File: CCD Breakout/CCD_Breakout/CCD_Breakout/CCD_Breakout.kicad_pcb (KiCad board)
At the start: 2 copper layers, 105.7 x 25.4 mm, 33 parts, among them U1 CCD, U3 ADC-MCP33151, U5 74HC541PW_118, U8 OPA4322AIPWR

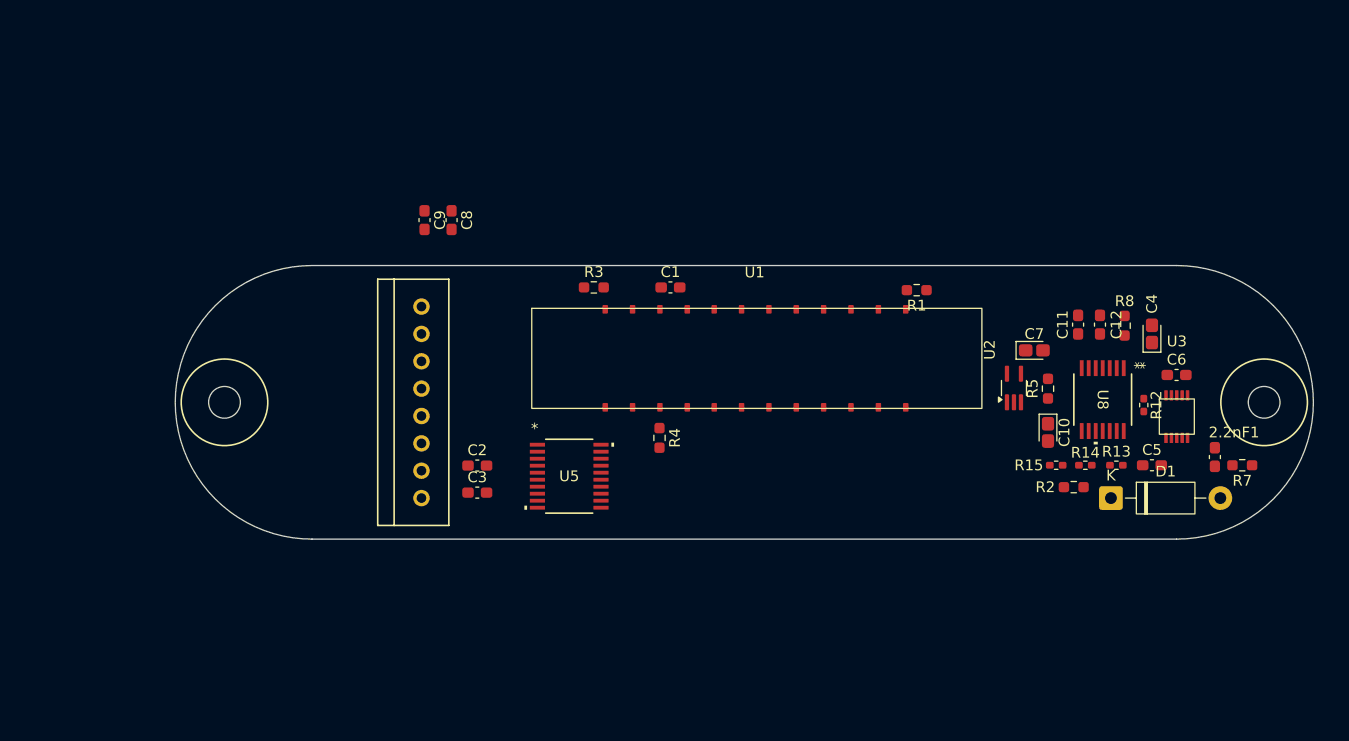
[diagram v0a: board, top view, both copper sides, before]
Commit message: CCD Positional Layout
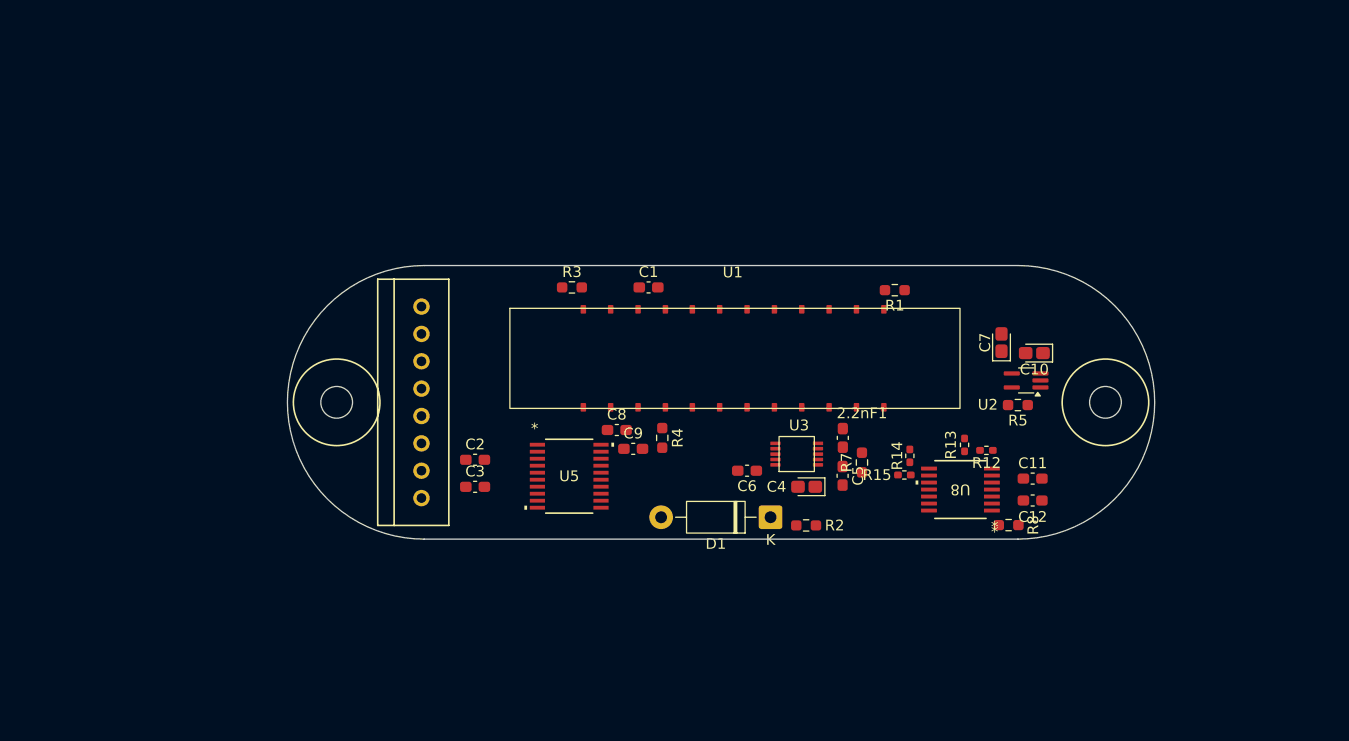
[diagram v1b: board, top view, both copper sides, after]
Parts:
- moved C6 40.9 mm to (147.8, 93.0), turned to 180 degrees
- moved U3 35.5 mm to (152.4, 91.4), turned to 90 degrees
- moved R7 35.3 mm to (158.5, 92.2), turned to 90 degrees
- moved C4 35.1 mm to (153.4, 94.5), turned to 180 degrees
- moved 2.2nF1 34.6 mm to (156.7, 89.9)
- moved D1 31.6 mm to (150.0, 97.3), turned to 180 degrees
- moved C9 28.7 mm to (137.3, 90.9), turned to 0 degrees
- moved C5 28.7 mm to (156.7, 93.4), turned to -90 degrees
- moved R2 25.1 mm to (153.3, 98.0), turned to 180 degrees
- moved C8 24.8 mm to (135.7, 89.2), turned to 0 degrees
- moved R8 21.4 mm to (172.1, 98.0), turned to 180 degrees
- moved C12 17.5 mm to (174.3, 95.7), turned to 0 degrees
- moved R14 16.3 mm to (162.9, 91.6), turned to 90 degrees
- moved U8 15.6 mm to (167.6, 94.7), turned to 180 degrees
- moved R12 15.2 mm to (170.1, 91.1), turned to 180 degrees
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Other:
- board size 105.7 x 25.4 mm -> 80.5 x 25.4 mm

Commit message: CCD Layout Traces
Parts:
- moved D1 0.83 mm to (149.4, 96.8)
- moved R2 0.83 mm to (152.7, 97.5)
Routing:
- net +5V: track 0.00 -> 164.6 mm, vias 0 -> 22
- net /ADC/OUT: track 0.00 -> 45.0 mm, vias 0 -> 3
- net +3V3: track 0.00 -> 43.6 mm, vias 0 -> 3
- net /ADC/CLK2: track 0.00 -> 43.1 mm, vias 0 -> 1
- net /CCD/EOSb: track 0.00 -> 41.1 mm, vias 0 -> 4
- net /CCD/opINA+: track 0.00 -> 25.9 mm, vias 0 -> 4
- net /CCD/EOS: track 0.00 -> 23.0 mm, vias 0 -> 1
- net /CCD/STb: track 0.00 -> 21.1 mm
- net /CCD/Trigb: track 0.00 -> 19.6 mm, vias 0 -> 2
- net /ADC/TRIG: track 0.00 -> 17.9 mm, vias 0 -> 2
- net /CCD/ST: track 0.00 -> 17.5 mm, vias 0 -> 1
- net /ADC/opIND+: track 0.00 -> 17.1 mm, vias 0 -> 3
- net /CCD/Videob: track 0.00 -> 15.6 mm, vias 0 -> 2
- net /ADC/opIND-: track 0.00 -> 14.1 mm, vias 0 -> 4
- net /CCD/opINB+: track 0.00 -> 13.9 mm
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- added copper zone on B.Cu, net GND
- added copper zone on F.Cu, net GND

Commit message: Added Reverse Voltage Protection
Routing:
- net (no net): vias 0 -> 2
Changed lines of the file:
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@@
+	)
+	(via
+		(at 80.772 51.562)
+		(size 0.6)
+		(drill 0.3)
+		(layers "F.Cu" "B.Cu")
+		(net 0)
+	)
+	(via
+		(at 201.422 75.184)
+		(size 0.6)
+		(drill 0.3)
+		(layers "F.Cu" "B.Cu")
+		(net 0)
 	)
 	(via

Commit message: Push
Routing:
- net GND: vias 46 -> 45
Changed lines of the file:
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@@
 		(layer "Edge.Cuts")
 	)
+	(dimension
+		(type orthogonal)
+		(layer "Dwgs.User")
+		(pts
+			(xy 185.674 86.614) (xy 105.156 86.614)
+		)
+		(height -18.034)
+		(orientation 0)
+		(format
+			(prefix "")
+			(suffix "")
+			(units 3)
+			(units_format 0)
+			(precision 4)
+			(suppress_zeroes yes)
+		)
+		(style
+			(thickness 0.1)
+			(arrow_length 1.27)
+			(text_position_mode 0)
+			(arrow_direction outward)
+			(extension_height 0.58642)
+			(extension_offset 0.5)
+			(keep_text_aligned yes)
+		)
+		(gr_text "3170"
+			(at 145.415 67.43 0)
+			(layer "Dwgs.User")
+			(effects
+				(font
+					(size 1 1)
+					(thickness 0.15)
+				)
+			)
+		)
+	)
+	(dimension
+		(type orthogonal)
+		(layer "Dwgs.User")
+		(pts
+			(xy 145.415 99.314) (xy 146.704 73.914)
+		)
+		(height 46.863)
+		(orientation 1)
+		(format
+			(prefix "")
+			(suffix "")
+			(units 3)
+			(units_format 0)
+			(precision 4)
+			(suppress_zeroes yes)
+		)
+		(style
+			(thickness 0.1)
+			(arrow_length 1.27)
+			(text_position_mode 0)
+			(arrow_direction outward)
+			(extension_height 0.58642)
+			(extension_offset 0.5)
+			(keep_text_aligned yes)
+		)
+		(gr_text "1000"
+			(at 191.128 86.614 90)
+			(layer "Dwgs.User")
+			(effects
+				(font
+					(size 1 1)
+					(thickness 0.15)
+				)
+			)
+		)
+	)
+	(dimension
+		(type orthogonal)
+		(layer "Dwgs.User")
+		(pts
+			(xy 181.102 86.614) (xy 109.728 86.614)
+		)
+		(height -22.352)
+		(orientation 0)
+		(format
+			(prefix "")
+			(suffix "")
+			(units 3)
+			(units_format 0)
+			(precision 4)
+			(suppress_zeroes yes)
+		)
+		(style
+			(thickness 0.1)
+			(arrow_length 1.27)
+			(text_position_mode 0)
+			(arrow_direction outward)
+			(extension_height 0.58642)
+			(extension_offset 0.5)
+			(keep_text_aligned yes)
+		)
+		(gr_text "2810"
+			(at 145.415 63.112 0)
+			(layer "Dwgs.User")
+			(effects
+				(font
+					(size 1 1)
+					(thickness 0.15)
+				)
+			)
+		)
+	)
 	(via
 		(at 80.772 51.562)
@@
 	)
 	(via
-		(at 179.324 80.01)
-		(size 0.6)
-		(drill 0.3)
-		(layers "F.Cu" "B.Cu")
-		(free yes)
-		(net 1)
-	)
-	(via
-		(at 126.492 94.742)
+		(at 179.324 79.502)
+		(size 0.6)
+		(drill 0.3)
+		(layers "F.Cu" "B.Cu")
+		(free yes)
+		(net 1)
+	)
+	(via
+		(at 126.238 95.504)
 		(size 0.6)
 		(drill 0.3)
@@
 	)
 	(via
-		(at 123.19 96.52)
+		(at 123.19 95.504)
 		(size 0.6)
 		(drill 0.3)
@@
 	)
 	(via
-		(at 154.686 89.154)
+		(at 154.686 88.392)
 		(size 0.6)
 		(drill 0.3)
@@
 	)
 	(via
-		(at 165.354 89.154)
+		(at 165.354 88.392)
 		(size 0.6)
 		(drill 0.3)
@@
 	)
 	(via
-		(at 179.832 93.218)
+		(at 179.324 93.218)
 		(size 0.6)
 		(drill 0.3)
@@
 	)
 	(via
-		(at 147.066 88.646)
-		(size 0.6)
-		(drill 0.3)
-		(layers "F.Cu" "B.Cu")
-		(free yes)
-		(net 1)
-	)
-	(via
-		(at 169.672 88.138)
+		(at 147.066 88.392)
+		(size 0.6)
+		(drill 0.3)
+		(layers "F.Cu" "B.Cu")
+		(free yes)
+		(net 1)
+	)
+	(via
+		(at 169.672 88.392)
 		(size 0.6)
 		(drill 0.3)
@@
 	)
 	(via
-		(at 141.224 91.948)
-		(size 0.6)
-		(drill 0.3)
-		(layers "F.Cu" "B.Cu")
-		(free yes)
-		(net 1)
-	)
-	(via
-		(at 163.83 82.55)
+		(at 143.51 91.948)
+		(size 0.6)
+		(drill 0.3)
+		(layers "F.Cu" "B.Cu")
+		(free yes)
+		(net 1)
+	)
+	(via
+		(at 163.83 82.296)
 		(size 0.6)
 		(drill 0.3)
@@
 	)
 	(via
-		(at 163.83 76.2)
-		(size 0.6)
-		(drill 0.3)
-		(layers "F.Cu" "B.Cu")
-		(free yes)
-		(net 1)
-	)
-	(via
-		(at 170.18 76.2)
-		(size 0.6)
-		(drill 0.3)
-		(layers "F.Cu" "B.Cu")
-		(free yes)
-		(net 1)
-	)
-	(via
-		(at 174.498 90.17)
+		(at 163.83 75.946)
+		(size 0.6)
+		(drill 0.3)
+		(layers "F.Cu" "B.Cu")
+		(free yes)
+		(net 1)
+	)
+	(via
+		(at 170.18 75.946)
+		(size 0.6)
+		(drill 0.3)
+		(layers "F.Cu" "B.Cu")
+		(free yes)
+		(net 1)
+	)
+	(via
+		(at 174.498 88.392)
 		(size 0.6)
 		(drill 0.3)
@@
 	)
 	(via
-		(at 151.13 88.9)
-		(size 0.6)
-		(drill 0.3)
-		(layers "F.Cu" "B.Cu")
-		(free yes)
-		(net 1)
-	)
-	(via
-		(at 143.51 90.424)
+		(at 151.13 88.392)
+		(size 0.6)
+		(drill 0.3)
+		(layers "F.Cu" "B.Cu")
+		(free yes)
+		(net 1)
+	)
+	(via
+		(at 143.51 88.392)
 		(size 0.6)
 		(drill 0.3)
@@
 	)
 	(via
-		(at 161.29 89.154)
+		(at 161.29 88.392)
 		(size 0.6)
 		(drill 0.3)
@@
 	(via
 		(at 121.412 77.216)
-		(size 0.6)
-		(drill 0.3)
-		(layers "F.Cu" "B.Cu")
-		(free yes)
-		(net 1)
-	)
-	(via
-		(at 158.75 89.154)
 		(size 0.6)
 		(drill 0.3)
@@
 		(min_thickness 0.25)
 		(filled_areas_thickness no)
-		(fill yes
+		(fill
 			(thermal_gap 0.5)
 			(thermal_bridge_width 0.5)
@@
 		(polygon
 			(pts
-				(xy 104.14 73.66) (xy 185.42 73.66) (xy 185.42 101.6) (xy 104.14 101.6)
+				(xy 104.14 73.66) (xy 186.182 73.66) (xy 186.182 100.1) (xy 104.14 100.1)
 			)
 		)

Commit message: CCD update
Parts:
- C8, C9, U5: moved to B.Cu
- moved R2 24.2 mm to (175.4, 105.8), turned to 90 degrees
- moved D1 23.0 mm to (166.6, 112.0)
- moved 2.2nF1 20.2 mm to (150.8, 109.3), turned to 0 degrees
- moved U3 20.0 mm to (146.3, 110.5)
- moved U5 19.7 mm to (149.4, 101.1), turned to 180 degrees
- moved C1 18.8 mm to (141.5, 94.5)
- moved R3 18.8 mm to (134.4, 94.5)
- moved R1 18.8 mm to (164.3, 94.7)
- moved U1 18.7 mm to (149.5, 101.1)
- moved C5 18.5 mm to (150.9, 111.0), turned to 0 degrees
- moved C4 18.5 mm to (150.8, 112.8), turned to 0 degrees
- moved C2 18.0 mm to (128.8, 108.8), turned to -90 degrees
- moved R4 17.8 mm to (141.4, 107.7), turned to 0 degrees
- moved R7 17.3 mm to (150.8, 107.7), turned to 180 degrees
- moved C3 16.3 mm to (130.6, 108.7), turned to -90 degrees
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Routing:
- net +5V: track 164.6 -> 128.4 mm, vias 22 -> 12
- net /CCD/EOSb: track 41.1 -> 9.70 mm, vias 4 -> 1
- net /ADC/opIND-: track 14.1 -> 37.9 mm, vias 4 -> 2
- net /CCD/EOS: track 23.0 -> 46.5 mm, vias 1 -> 3
- net /ADC/OUT: track 45.0 -> 23.3 mm, vias 3 -> 4
- net /CCD/CLK: track 13.6 -> 34.4 mm, vias 1 -> 2
- net /CCD/ST: track 17.5 -> 35.3 mm, vias 1 -> 4
- net /ADC/Video: track 8.39 -> 24.9 mm
- net /CCD/Videob: track 15.6 -> 1.63 mm, vias 2 -> 0
- net +3V3: track 43.6 -> 29.6 mm
- net /CCD/opINB-: track 2.38 -> 14.8 mm, vias 0 -> 4
- net /CCD/opINA+: track 25.9 -> 16.2 mm, vias 4 -> 2
- net /ADC/CLK2: track 43.1 -> 33.7 mm, vias 1 -> 3
- net /CCD/opINC-: track 2.93 -> 12.1 mm, vias 0 -> 3
- net /CCD/CLKb: track 6.37 -> 15.1 mm, vias 2 -> 3
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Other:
- board size 80.5 x 25.4 mm -> 73.9 x 25.4 mm
- board text added: "ADC"
- board text added: "Octal Buffer"
- board text added: "V Shifter"

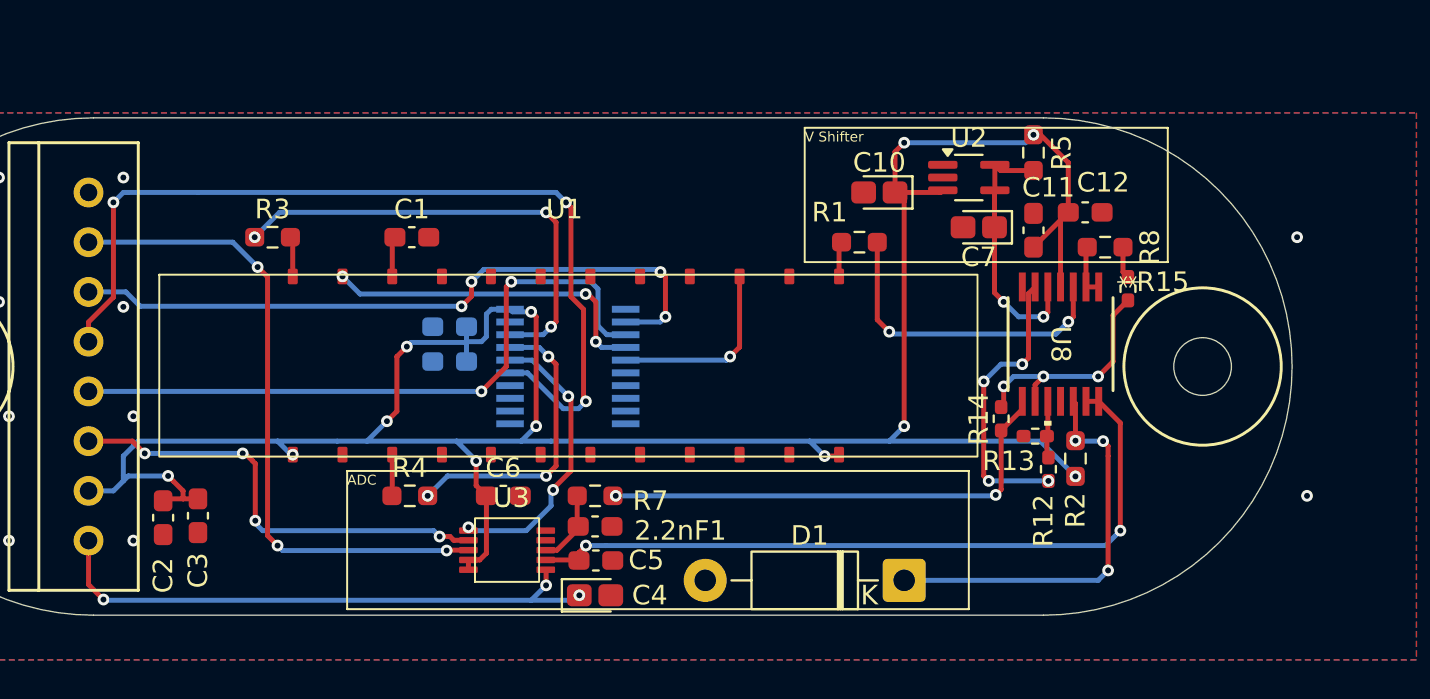
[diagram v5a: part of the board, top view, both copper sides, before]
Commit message: Fix Resistor Footprints
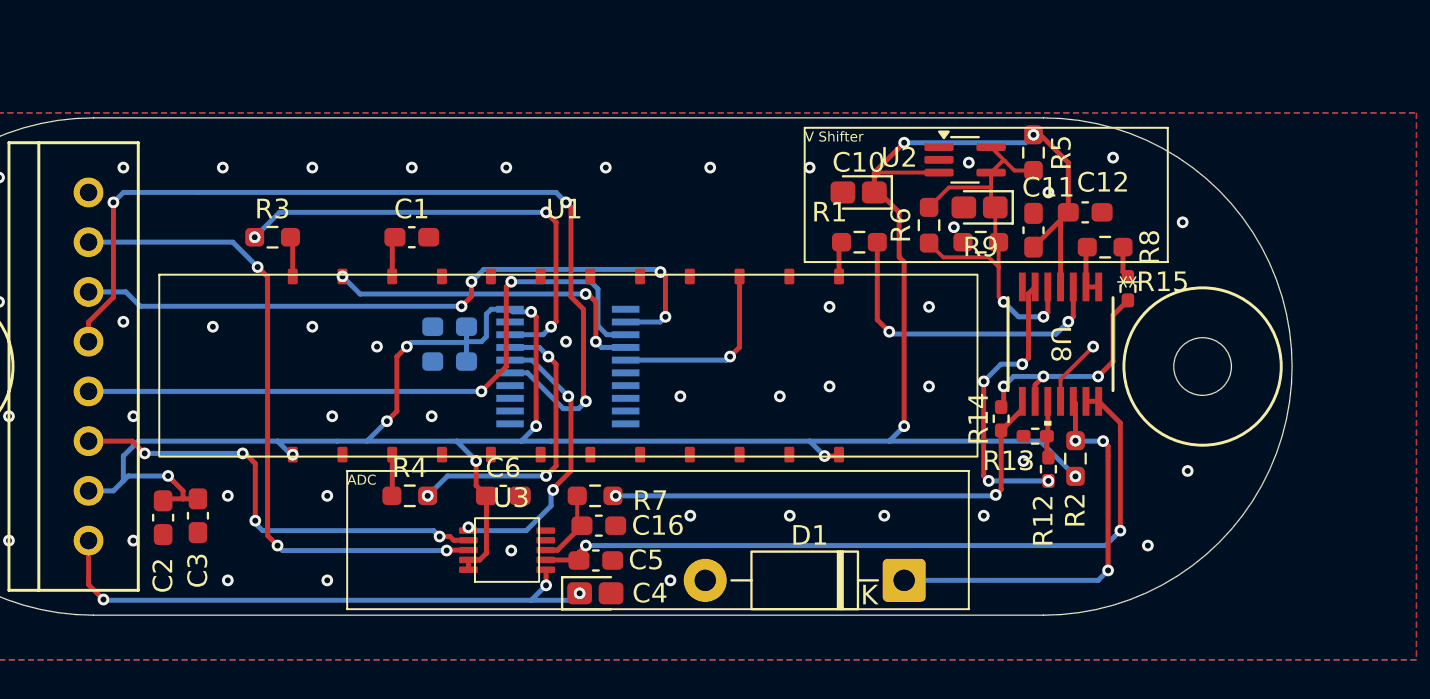
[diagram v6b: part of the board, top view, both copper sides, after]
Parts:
- removed 2.2nF1: C, Capacitor_SMD:C_0603_1608Metric_Pad1.08x0.95mm_HandSolder
- added C16: 2.2nF, Capacitor_SMD:C_0603_1608Metric_Pad1.08x0.95mm_HandSolder, F.Cu at (151.0, 109.2)
- added R6: 10k, Resistor_SMD:R_0603_1608Metric_Pad0.98x0.95mm_HandSolder, F.Cu at (167.9, 93.9)
- added R9: 15k, Resistor_SMD:R_0603_1608Metric_Pad0.98x0.95mm_HandSolder, F.Cu at (170.5, 94.7)
- C7: value 1uF -> 0.47uF
- R2: value 1000 -> 1k
- moved C10 1.06 mm to (164.3, 92.2)
- moved C7 1.02 mm to (170.5, 93.0)
- moved U2 0.92 mm to (169.7, 90.5)
- moved C4 0.10 mm to (150.8, 112.7)
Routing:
- net /CCD/opINB+: track 13.3 -> 22.1 mm
- net GND: track 0.00 -> 3.48 mm, vias 10 -> 46
- net +5V: track 128.4 -> 130.4 mm

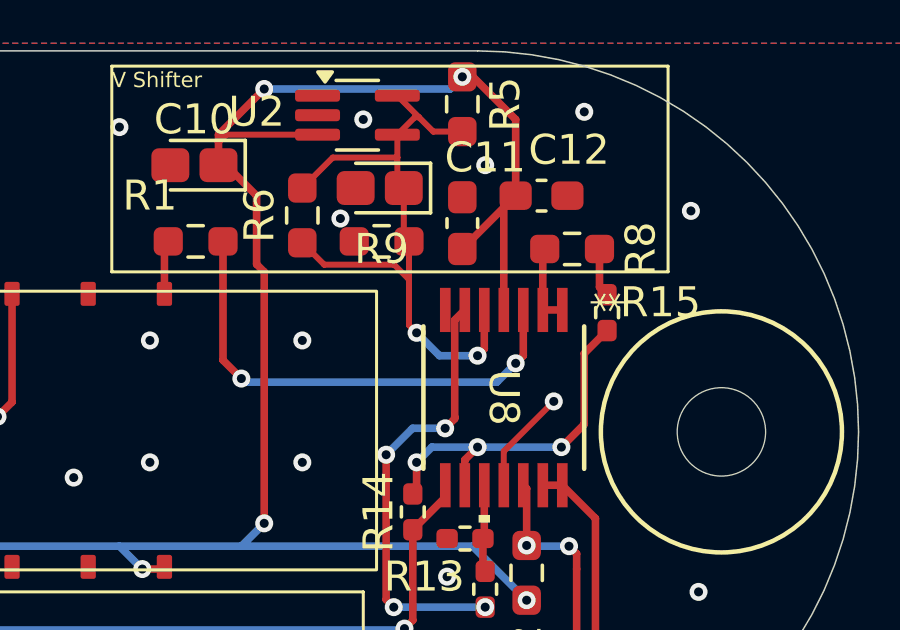
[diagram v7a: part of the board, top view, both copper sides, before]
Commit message: Trace Width Fix
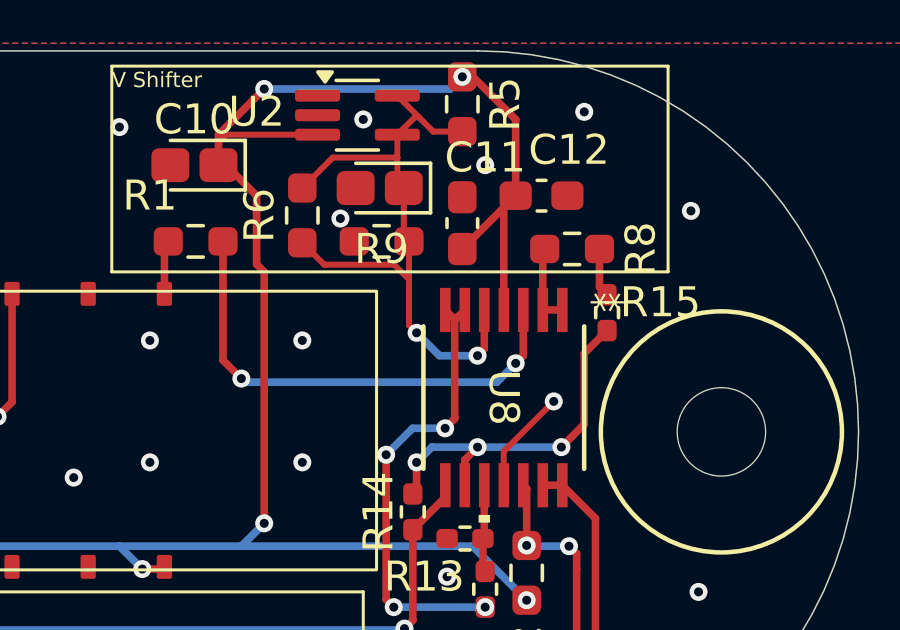
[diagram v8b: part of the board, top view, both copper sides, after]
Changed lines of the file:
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@@
+	)
+	(segment
+		(start 172.974 97.341998)
+		(end 172.660002 97.028)
+		(width 0.254)
+		(layer "F.Cu")
+		(net 18)
 	)
 	(segment
@@
 		(width 0.254)
 		(layer "F.Cu")
+		(net 18)
+	)
+	(segment
+		(start 172.974 97.364001)
+		(end 172.974 97.341998)
+		(width 0.254)
+		(layer "F.Cu")
